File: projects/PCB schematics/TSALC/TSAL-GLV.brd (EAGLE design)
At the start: 160 x 100 mm, 15 parts, among them IC1 74AHC1G04DBV, IC3 74AUC1G17DBV, IC4 NE555D, Q1 IRLZ44Z, Q2 IRLZ44Z, Q3 IRLZ44Z

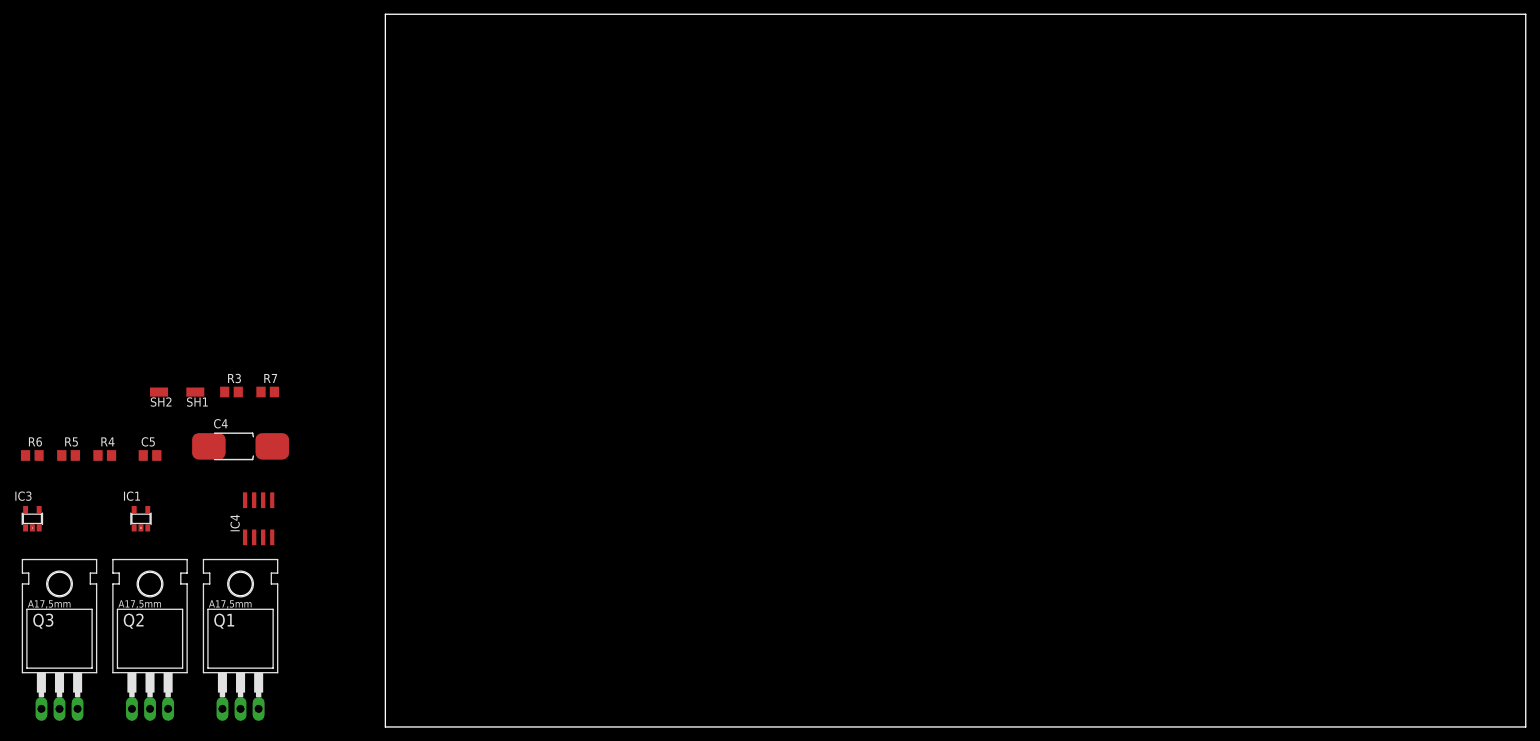
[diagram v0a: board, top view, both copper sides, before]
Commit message: TSALC - GLV board completed.
Preliminary layout completed for GLV. Must silkscreen and double check connections between GLV and TS boards.

Squash - TSALC - Silkscreen additions.
Initial silkscreen work done. Inputs and outputs must be annotated.
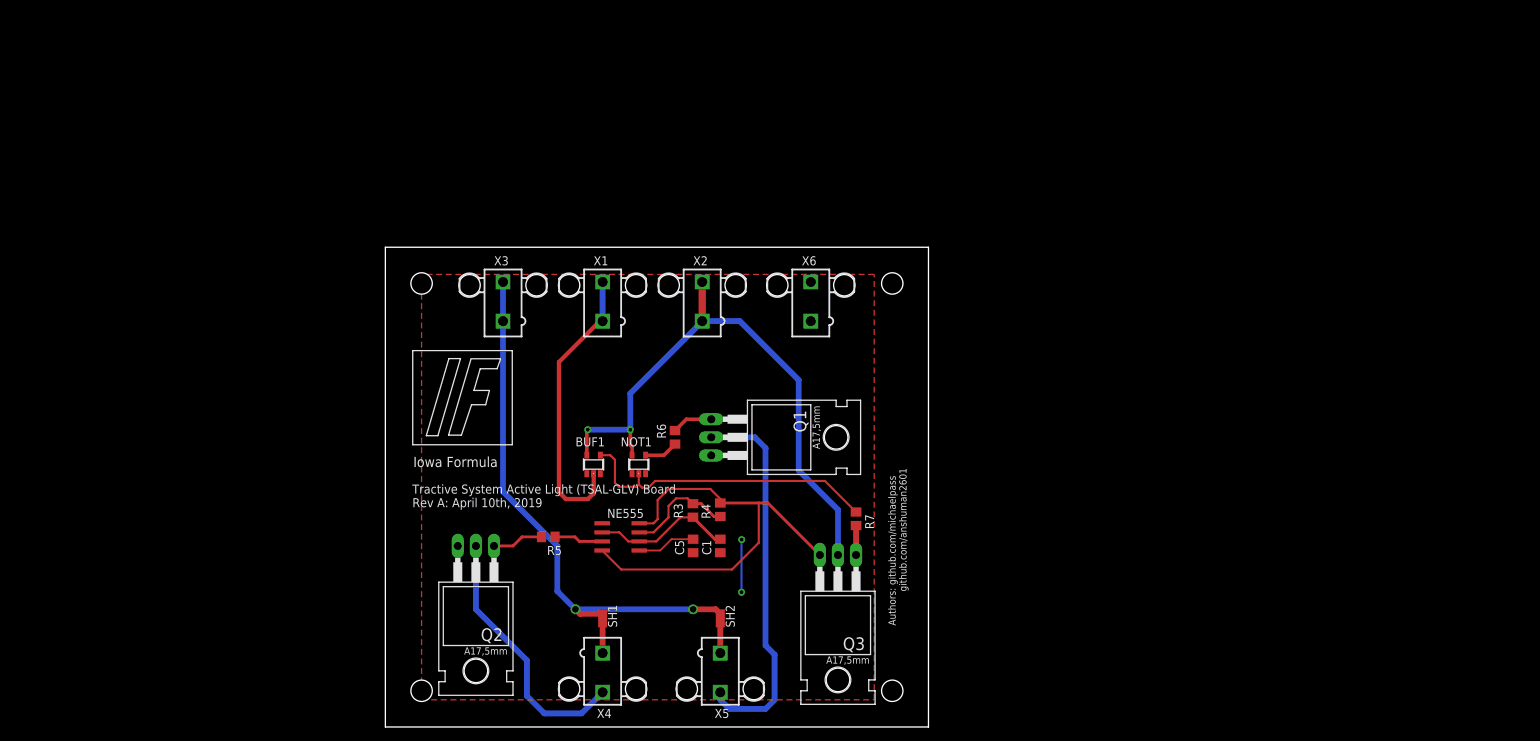
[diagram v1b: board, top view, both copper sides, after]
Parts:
- removed C4: 4.7uF, rcl:085CS_1AW
- removed IC1: 74AHC1G04DBV, 74xx-little-us:SOT23-5
- removed IC3: 74AUC1G17DBV, 74xx-little-us:SOT23-5
- removed IC4: NE555D, linear:SO08
- added BUF1: 74AUC1G17DBV, 74xx-little-us:SOT23-5
- added C1: 4.7uF, rcl:C0805
- added NE555: NE555D, linear:SO08
- added NOT1: 74AHC1G04DBV, 74xx-little-us:SOT23-5
- added X1, X2, X3, X4, X5, X6: 5566-2, con-molex:5566-2
- moved Q3 109.6 mm to (63.5, 17.8), turned to 180 degrees
- moved R6 90.2 mm to (40.6, 40.6), turned to 90 degrees
- moved R4 86.7 mm to (47.0, 30.5), turned to 270 degrees
- moved SH2 84.9 mm to (47.0, 15.2), turned to 90 degrees
- moved R7 84.4 mm to (66.0, 29.2), turned to 270 degrees
- moved Q1 79.0 mm to (52.1, 40.6), turned to 270 degrees
- moved C5 77.3 mm to (43.2, 25.4), turned to 90 degrees
- moved R5 68.3 mm to (22.9, 26.7), turned to 180 degrees
- moved R3 66.8 mm to (43.2, 30.4), turned to 270 degrees
- moved SH1 65.4 mm to (30.5, 15.2), turned to 90 degrees
- moved Q2 46.8 mm to (12.7, 19.1), turned to 180 degrees
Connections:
- removed net N$13: IC3.2
- new net TSAL_CONTROL_SIGNAL: BUF1.2, X1.1, X1.2
- net +12V-ISO: now also X3.1, X3.2
- net +60VDANGER-FLASHRED: now also BUF1.4, NOT1.2; no longer IC1.2, IC3.4
- net GND: now also BUF1.3, C1.2, NE555.1, NOT1.3, X6.1, X6.2; no longer C4.-, IC1.3, IC3.3, IC4.1
- net GREEN_LED-: now also X5.2
- net GREEN_LED_RESISTOR+: now also X5.1
- net N$1: now also NE555.3; no longer IC4.3
- net N$2: now also NE555.7; no longer IC4.7
- net N$7: now also NE555.5; no longer IC4.5
- net RED_LED-: now also X4.2
- net RED_LED_RESISTOR+: now also X4.1
- net SAFESIGNAL-SOLIDGREEN: now also NOT1.4; no longer IC1.4
- net THR: now also C1.1, NE555.2, NE555.6; no longer C4.+, IC4.2, IC4.6
- net VCC: now also BUF1.5, NOT1.5, X2.1, X2.2; no longer IC1.5, IC3.5
- net VTIMER: now also NE555.4, NE555.8; no longer IC4.4, IC4.8
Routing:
- net VCC: track 0.00 -> 82.0 mm, vias 0 -> 2
- net +12V-ISO: track 0.00 -> 74.8 mm, vias 0 -> 2
- net VTIMER: track 0.00 -> 63.3 mm
- net GREEN_LED-: track 0.00 -> 53.8 mm
- net +60VDANGER-FLASHRED: track 0.00 -> 43.6 mm
- net TSAL_CONTROL_SIGNAL: track 0.00 -> 40.6 mm
- net RED_LED-: track 0.00 -> 36.9 mm
- net THR: track 0.00 -> 19.8 mm
- net N$2: track 0.00 -> 15.3 mm
- net N$7: track 0.00 -> 8.22 mm
- net GND: track 0.00 -> 7.40 mm, vias 0 -> 2
- net N$8: track 0.00 -> 7.20 mm
- net N$1: track 0.00 -> 6.94 mm
- net N$14: track 0.00 -> 5.74 mm
- net SAFESIGNAL-SOLIDGREEN: track 0.00 -> 4.78 mm
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- added copper zone on layer 1, net GND
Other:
- board size 160 x 100 mm -> 76.2 x 67.3 mm
- board text added: "Authors: github.com/michaelpass github.com/anshuman2601"
- board text added: "Iowa Formula"
- board text added: "Tractive System Active Light (TSAL-GLV) Board Rev A: April 10th, 2019"

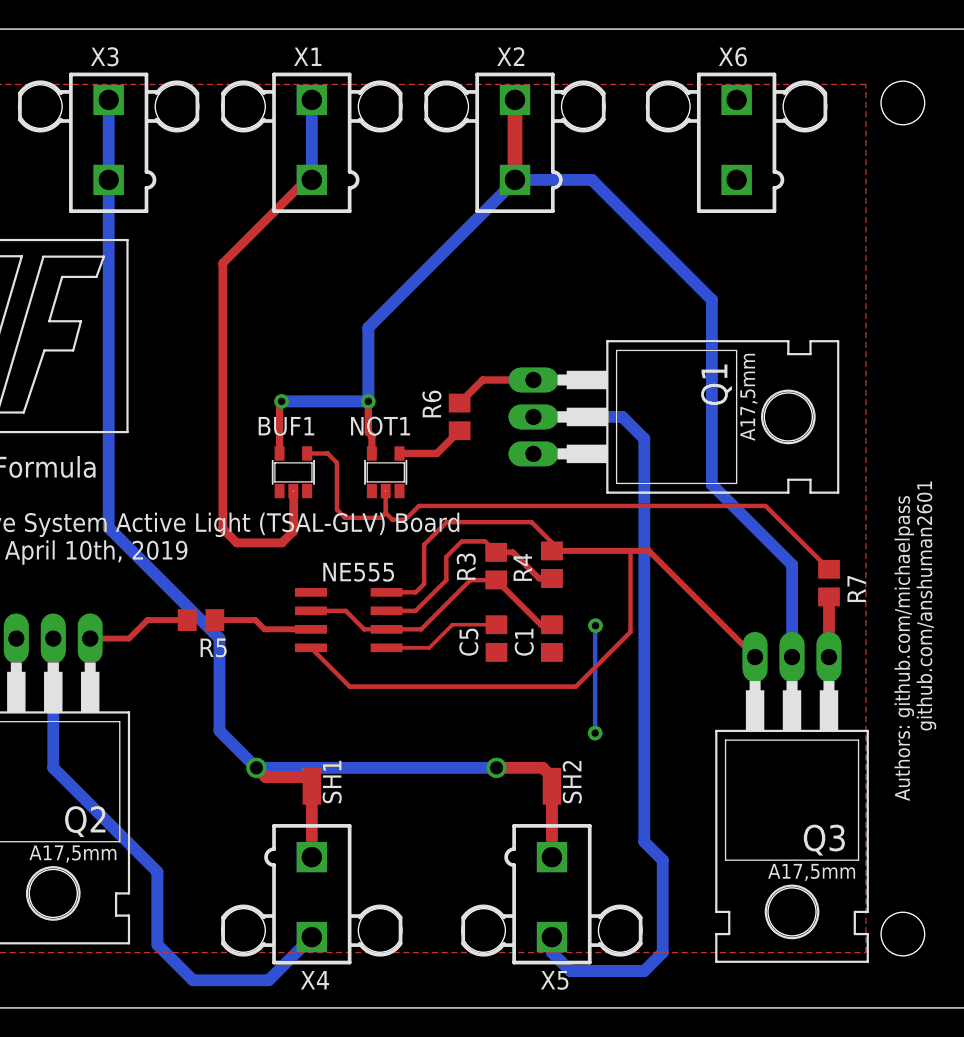
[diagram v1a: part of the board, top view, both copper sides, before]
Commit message: TSALC - GLV; Rev A.
GLV ready for pull request review.
This board has nothing but GLV components on it.
Interface to TS board occurs between VCC and TSAL_CONTROL_SIGNAL

Squash - TSALC - GLV; Added pull-down resistor to input.
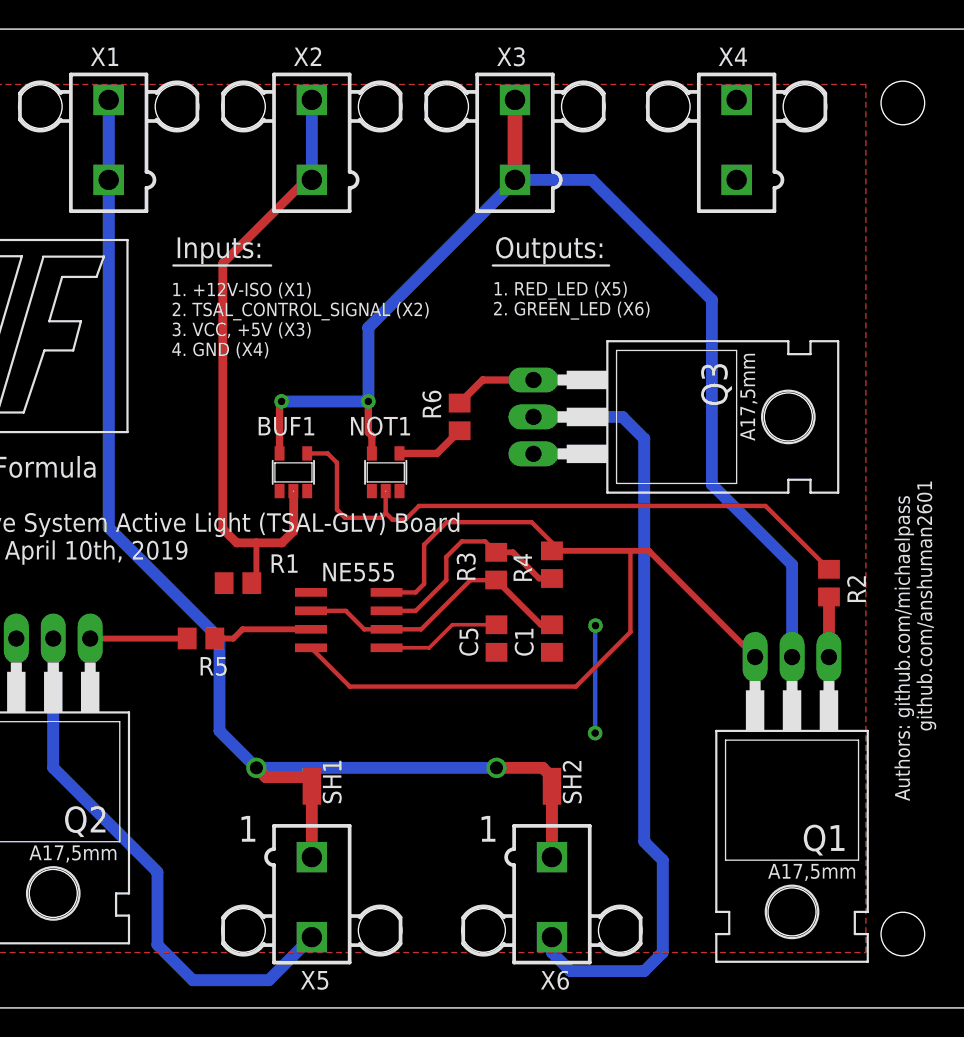
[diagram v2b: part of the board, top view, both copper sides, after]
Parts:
- added R1: 10k, rcl:R0805
- moved X4 59.7 mm to (59.7, 59.7), turned to 0 degrees
- moved X6 53.6 mm to (47.0, 7.62), turned to 180 degrees
- moved X3 27.9 mm to (44.5, 59.7)
- moved Q1 25.6 mm to (63.5, 17.8), turned to 180 degrees
- moved Q3 25.6 mm to (52.1, 40.6), turned to 270 degrees
- moved X5 16.5 mm to (30.5, 7.62)
- moved X2 14.0 mm to (30.5, 59.7)
- moved X1 14.0 mm to (16.5, 59.7)
- moved R5 1.27 mm to (22.9, 25.4)
- renumbered R7 to R2
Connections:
- net +12V-ISO: now also X1.1, X1.2; no longer X3.1, X3.2
- net GND: now also Q3.S, R1.2, X4.1, X4.2; no longer Q1.S, X6.1, X6.2
- net GREEN_LED-: now also Q3.D, X6.2; no longer Q1.D, X5.2
- net GREEN_LED_RESISTOR+: now also X6.1; no longer X5.1
- net N$11: now also Q1.G; no longer Q3.G
- net N$14: now also Q3.G; no longer Q1.G
- net RED_LED-: now also X5.2; no longer X4.2
- net RED_LED_RESISTOR+: now also X5.1; no longer X4.1
- net TSAL_CONTROL_SIGNAL: now also R1.1, X2.1, X2.2; no longer X1.1, X1.2
- net VCC: now also Q1.D, X3.1, X3.2; no longer Q3.D, X2.1, X2.2
- net VTIMER: now also Q1.S; no longer Q3.S
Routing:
- net TSAL_CONTROL_SIGNAL: track 40.6 -> 43.5 mm
- net N$8: track 7.20 -> 6.67 mm
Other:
- board text added: "1"
- board text added: "1. +12V-ISO (X1) 2. TSAL_CONTROL_SIGNAL (X2) 3. VCC, +5V (X3) 4. GND (X4)"
- board text added: "1. RED_LED (X5) 2. GREEN_LED (X6)"
- board text added: "Inputs:"
- board text added: "Outputs:"

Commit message: TSAL - Resizing.
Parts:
- moved Q1 18.1 mm to (74.9, 31.8)
- moved X4 18.1 mm to (71.1, 73.7)
- moved BUF1 18.1 mm to (40.6, 50.8)
- moved C1 18.1 mm to (58.4, 39.4)
- moved C5 18.1 mm to (54.6, 39.4)
- moved NE555 18.1 mm to (44.5, 40.6)
- moved NOT1 18.1 mm to (47.0, 50.8)
- moved Q2 18.1 mm to (24.1, 33.0)
- moved Q3 18.1 mm to (63.5, 54.6)
- moved R1 18.1 mm to (36.8, 43.2)
- moved R3 18.1 mm to (54.6, 44.3)
- moved R4 18.1 mm to (58.4, 44.5)
- moved R5 18.1 mm to (34.3, 39.4)
- moved R6 18.1 mm to (52.1, 54.6)
- moved SH2 18.1 mm to (58.4, 29.2)
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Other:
- board size 76.2 x 67.3 mm -> 99.1 x 99.1 mm

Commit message: PROJ - Final pre-purchase revisions (4 boards still in progress.)
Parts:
- removed X1, X2, X3, X4, X5, X6: 5566-2, con-molex:5566-2
- added +12V-ISO.1, GND.1, GREEN_LED, RED_LED, TSAL_CONTROL_SIGNAL, VCC.1: 5566-2, con-molex:5566-2
- moved BUF1 4.58 mm to (44.5, 53.3)
- moved C5 4.58 mm to (58.4, 41.9)
- moved Q2 4.58 mm to (27.9, 35.6)
- moved Q3 4.58 mm to (67.3, 57.1)
- moved R1 4.58 mm to (40.6, 45.7)
- moved R2 4.58 mm to (81.3, 45.7)
- moved R5 4.58 mm to (38.1, 41.9)
- moved R6 4.58 mm to (55.9, 57.1)
- moved SH1 4.58 mm to (45.7, 31.8)
- moved NOT1 4.58 mm to (50.8, 53.3)
- moved C1 4.58 mm to (62.2, 41.9)
- moved NE555 4.58 mm to (48.3, 43.2)
- moved R3 4.58 mm to (58.4, 46.9)
- moved R4 4.58 mm to (62.2, 47.0)
- moved SH2 4.58 mm to (62.2, 31.8)
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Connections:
- net +12V-ISO: now also +12V-ISO.1.1, +12V-ISO.1.2; no longer X1.1, X1.2
- net GND: now also GND.1.1, GND.1.2; no longer X4.1, X4.2
- net GREEN_LED-: now also GREEN_LED.2; no longer X6.2
- net GREEN_LED_RESISTOR+: now also GREEN_LED.1; no longer X6.1
- net RED_LED-: now also RED_LED.2; no longer X5.2
- net RED_LED_RESISTOR+: now also RED_LED.1; no longer X5.1
- net TSAL_CONTROL_SIGNAL: now also TSAL_CONTROL_SIGNAL.1, TSAL_CONTROL_SIGNAL.2; no longer X2.1, X2.2
- net VCC: now also VCC.1.1, VCC.1.2; no longer X3.1, X3.2
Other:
- board text added: "GREEN_LED: 1. GREEN_LED_RESISTOR+ 2. GREEN_LED-"
- board text added: "RED_LED: 1. RED_LED_RESISTOR+ 2. RED_LED-"

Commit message: PROJ - Gerber files major milestone - 05/05/19.
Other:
- board text added: "Tractive System Active Light (TSAL-GLV) Board Rev A: May 5th, 2019"
- board text removed: "Tractive System Active Light (TSAL-GLV) Board Rev A: April 10th, 2019"
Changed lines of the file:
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@@
 <text x="19.1516" y="52.9844" size="1.4224" layer="25" font="vector">Iowa Formula</text>
 <text x="13.9446" y="47.3456" size="1.27" layer="25" font="vector">Tractive System Active Light (TSAL-GLV) Board
-Rev A: April 10th, 2019</text>
+Rev A: May 5th, 2019</text>
 <text x="88.3666" y="30.734" size="1.016" layer="25" font="vector" rot="R90">Authors: github.com/michaelpass
             github.com/anshuman2601             </text>
@@
 <signals>
 <signal name="GND">
-<contactref element="NOT1" pad="3"/>
-<contactref element="BUF1" pad="3"/>
 <contactref element="NE555" pad="1"/>
 <contactref element="C5" pad="1"/>
@@
 <wire x1="65.2018" y1="42.7736" x2="65.2018" y2="35.4076" width="0.3048" layer="16"/>
 <contactref element="R1" pad="2"/>
+<contactref element="BUF1" pad="3"/>
+<contactref element="NOT1" pad="3"/>
 </signal>
 <signal name="VCC">
-<contactref element="NOT1" pad="5"/>
-<contactref element="BUF1" pad="5"/>
 <contactref element="Q1" pad="D"/>
 <contactref element="VCC.1" pad="1"/>
@@
 <wire x1="49.6062" y1="63.2968" x2="49.6062" y2="58.2168" width="0.8128" layer="16"/>
 <via x="49.6062" y="58.2168" extent="1-16" drill="0.508"/>
-<wire x1="49.6062" y1="58.2168" x2="49.6062" y2="56.0832" width="0.508" layer="1"/>
-<wire x1="49.85" y1="55.8394" x2="49.85" y2="54.64" width="0.508" layer="1"/>
-<wire x1="49.6062" y1="56.0832" x2="49.85" y2="55.8394" width="0.508" layer="1"/>
+<wire x1="49.85" y1="54.64" x2="49.8602" y2="54.6502" width="0.508" layer="1"/>
+<wire x1="49.6062" y1="58.2168" x2="49.8602" y2="57.9628" width="0.508" layer="1"/>
+<wire x1="49.8602" y1="57.9628" x2="49.8602" y2="54.6502" width="0.508" layer="1"/>
 <via x="43.6372" y="58.2168" extent="1-16" drill="0.508"/>
-<wire x1="43.6372" y1="58.2168" x2="43.5" y2="58.0796" width="0.508" layer="1"/>
-<wire x1="43.5" y1="58.0796" x2="43.5" y2="54.64" width="0.508" layer="1"/>
+<contactref element="BUF1" pad="5"/>
+<wire x1="43.6372" y1="58.2168" x2="43.5102" y2="58.0898" width="0.508" layer="1"/>
+<wire x1="43.5102" y1="58.0898" x2="43.5102" y2="54.6502" width="0.508" layer="1"/>
+<wire x1="43.5102" y1="54.6502" x2="43.5" y2="54.64" width="0.508" layer="1"/>
+<contactref element="NOT1" pad="5"/>
 </signal>
 <signal name="+12V-ISO">
